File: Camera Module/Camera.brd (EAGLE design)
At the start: 39.7 x 23 mm, 7 parts, among them U2 RFM69HCW

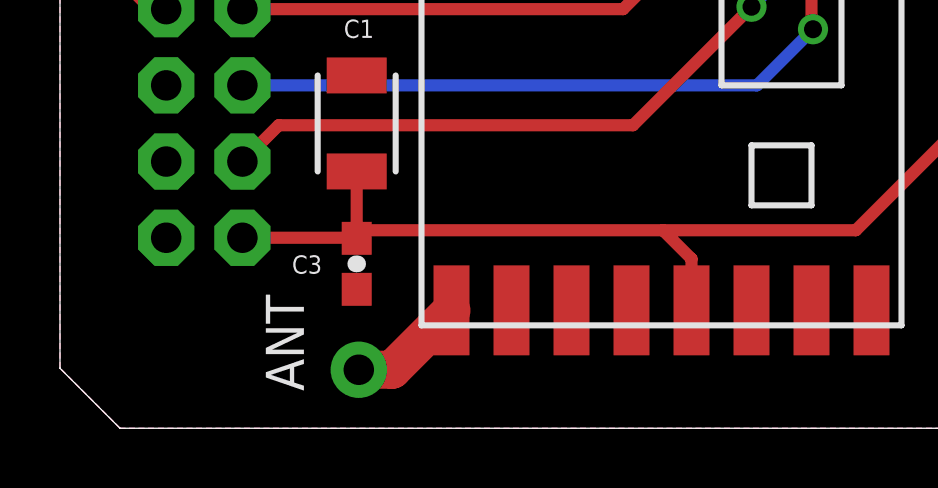
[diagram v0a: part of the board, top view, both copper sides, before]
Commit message: Added the interrupt line from the RFM69 into the Camera Module board. It is connected to GPIO_24
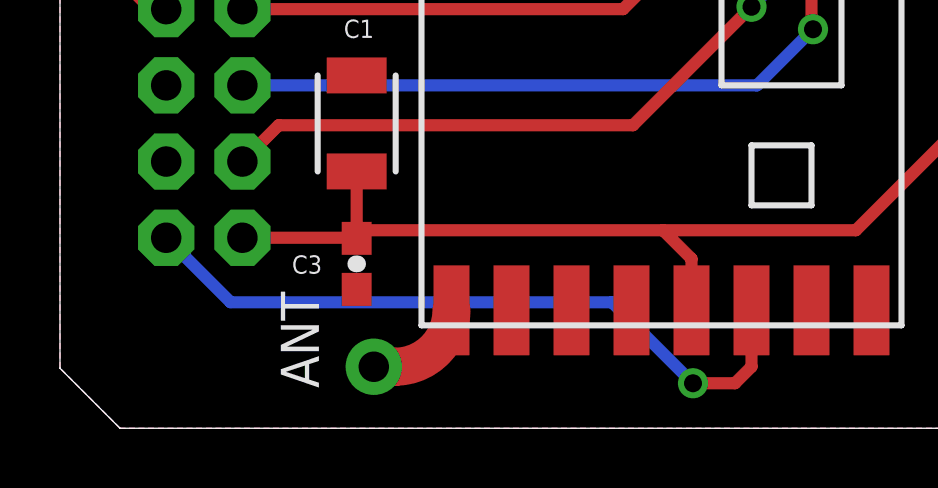
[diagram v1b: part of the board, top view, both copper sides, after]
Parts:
- moved ANT 0.51 mm to (10.5, 2.05)
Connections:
- new net INT: J1.2, U2.14
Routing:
- net INT: track 0.00 -> 23.6 mm, vias 0 -> 1
- net ANT: track 3.91 -> 3.37 mm
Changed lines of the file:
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@@
 </autorouter>
 <elements>
-<element name="ANT" library="SparkFun-Connectors" package="1X01_NO_SILK" value="" x="9.96" y="1.95" smashed="yes" rot="R90">
-<attribute name="NAME" x="8.1312" y="1.2438" size="1.27" layer="25" rot="R90"/>
-<attribute name="VALUE" x="13.135" y="0.68" size="1.27" layer="27" rot="R90"/>
+<element name="ANT" library="SparkFun-Connectors" package="1X01_NO_SILK" value="" x="10.46" y="2.05" smashed="yes" rot="R90">
+<attribute name="NAME" x="8.6312" y="1.3438" size="1.27" layer="25" rot="R90"/>
+<attribute name="VALUE" x="13.635" y="0.78" size="1.27" layer="27" rot="R90"/>
 </element>
 <element name="C1" library="SparkFun-Capacitors" package="1210" value="10uF" x="9.89" y="10.16" smashed="yes" rot="R90">
@@
 <contactref element="U2" pad="9"/>
 <contactref element="ANT" pad="1"/>
-<wire x1="9.96" y1="1.95" x2="11.07" y2="1.95" width="1.27" layer="1"/>
-<wire x1="11.07" y1="1.95" x2="13.05" y2="3.93" width="1.27" layer="1"/>
+<wire x1="10.46" y1="2.05" x2="11.17" y2="2.05" width="1.27" layer="1"/>
+<wire x1="11.17" y1="2.05" x2="13.05" y2="3.93" width="1.27" layer="1" curve="90"/>
 </signal>
 <signal name="MOSI">
@@
 <contactref element="J1" pad="10"/>
 </signal>
+<signal name="INT">
+<contactref element="U2" pad="14"/>
+<contactref element="J1" pad="2"/>
+<via x="21.1" y="1.5" extent="1-16" drill="0.6"/>
+<wire x1="23.05" y1="3.93" x2="23.05" y2="2.05" width="0.4064" layer="1"/>
+<wire x1="23.05" y1="2.05" x2="22.5" y2="1.5" width="0.4064" layer="1"/>
+<wire x1="22.5" y1="1.5" x2="21.1" y2="1.5" width="0.4064" layer="1"/>
+<wire x1="21.1" y1="1.5" x2="18.4" y2="4.2" width="0.4064" layer="16"/>
+<wire x1="18.4" y1="4.2" x2="5.69" y2="4.2" width="0.4064" layer="16"/>
+<wire x1="5.69" y1="4.2" x2="3.54" y2="6.35" width="0.4064" layer="16"/>
+</signal>
 </signals>

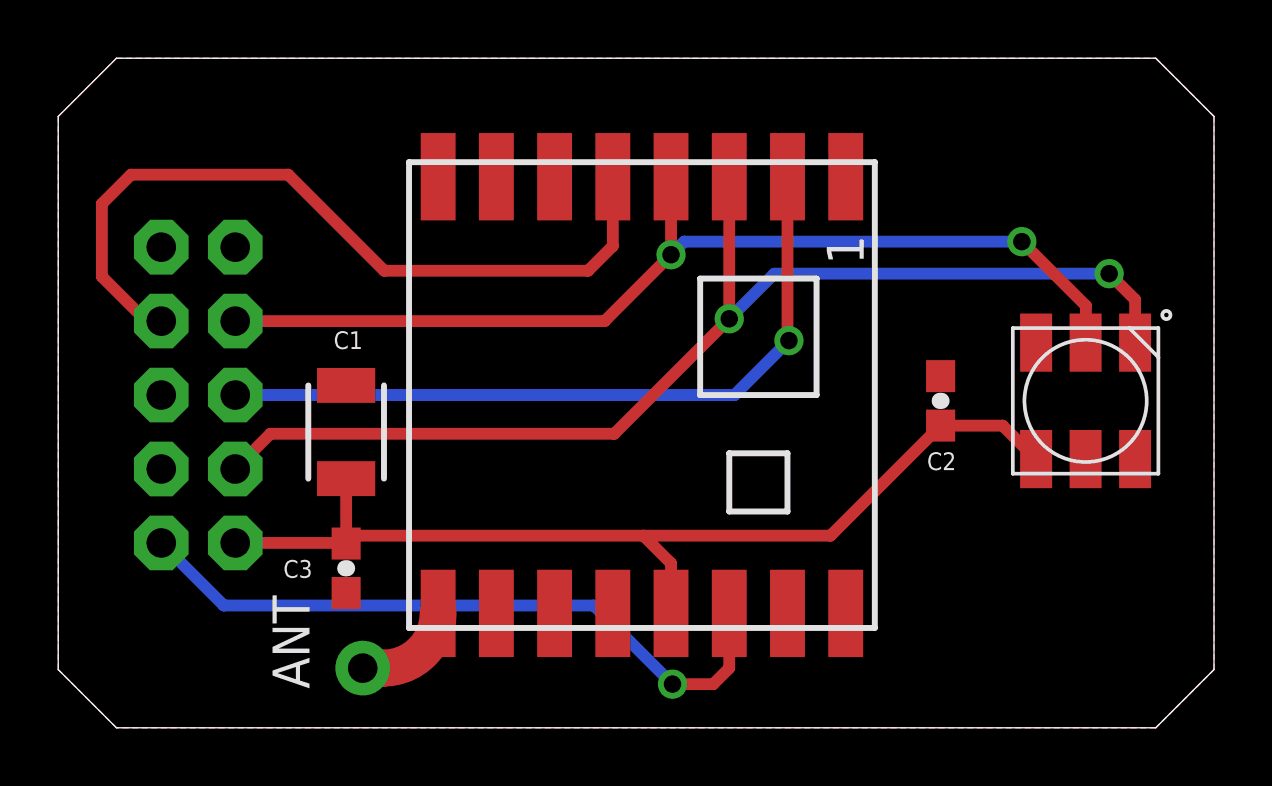
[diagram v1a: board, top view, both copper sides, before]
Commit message: Update the camera module board to include a chip select line for the APA102 and added to the silk screen
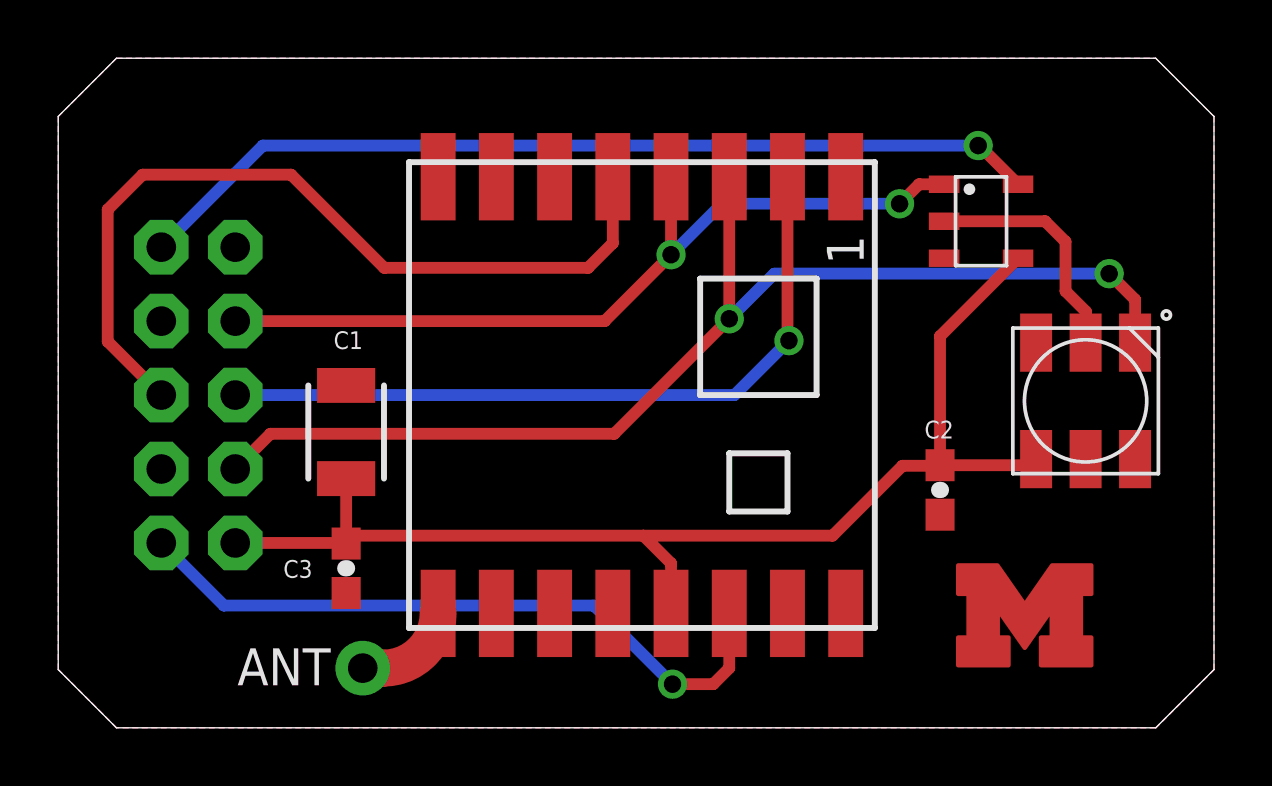
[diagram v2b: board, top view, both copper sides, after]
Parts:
- added U$2: TS12A4514, SAUVE:SOT-23
- added U$3: (no value), MAAV_BlockM:BLOCK-M-5MM-MASK
- added U$5: (no value), MAAV_BlockM:BLOCK-M-10MM
- moved C2 3.06 mm to (30.3, 8.17), turned to 270 degrees
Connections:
- net INT renamed GPIO24
- new net APA_SCLK: U$1.CKI, U$2.2
- new net GPIO25: J1.6, U2.5
- net 3.3V: now also U$2.4
- net CE0: no longer U2.5
- net CE1: now also U$2.5
- net GND: now also U$2.3
- net SCLK: now also U$2.1; no longer U$1.CKI
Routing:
- net CE1: track 0.00 -> 31.4 mm, vias 0 -> 1
- net GPIO25: track 0.00 -> 28.9 mm
- net CE0: track 27.2 -> 0.00 mm
- net APA_SCLK: track 0.00 -> 8.22 mm
- net 3.3V: track 35.0 -> 42.3 mm
- net SCLK: track 34.5 -> 29.0 mm
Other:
- board text added: "AIZER"
- board text added: "Camera Module"
- board text added: "Designed By: Matt Sauvé"

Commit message: Finalized all PCBs
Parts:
- added JP1: JUMPER-PAD-2-NC_BY_TRACE, SparkFun-Passives:PAD-JUMPER-2-NC_BY_TRACE_YES_SILK
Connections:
- net APA_SCLK: now also JP1.2
- net SCLK: now also JP1.1
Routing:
- net SCLK: track 29.0 -> 37.4 mm
- net APA_SCLK: track 8.22 -> 11.0 mm
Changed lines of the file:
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@@
 <wire x1="0" y1="2" x2="2" y2="0" width="0" layer="20"/>
 <text x="28.5" y="7.4" size="5.08" layer="22" ratio="12" rot="MR0">AIZER</text>
-<text x="38.6" y="5.5" size="1.27" layer="22" ratio="12" rot="MR0">Camera Module</text>
+<text x="38.6" y="5.1" size="1.27" layer="22" ratio="12" rot="MR0">Camera Module</text>
 <text x="37.1" y="1.3" size="0.6096" layer="22" ratio="10" rot="MR0">Designed By: Matt Sauvé</text>
 </plain>
@@
 </class>
 </classes>
-<designrules name="default">
+<designrules name="oshpark-2layer">
 <description language="de">&lt;b&gt;EAGLE Design Rules&lt;/b&gt;
 &lt;p&gt;
@@
 Einstellungen hier und speichern die Design Rules unter
 einem neuen Namen ab.</description>
-<description language="en">&lt;b&gt;EAGLE Design Rules&lt;/b&gt;
+<description language="en">&lt;b&gt;Laen's PCB Order Design Rules&lt;/b&gt;
 &lt;p&gt;
-The default Design Rules have been set to cover
-a wide range of applications. Your particular design
-may have different requirements, so please make the
-necessary adjustments and save your customized
-design rules under a new name.</description>
+Please make sure your boards conform to these design rules.</description>
 <param name="layerSetup" value="(1*16)"/>
-<param name="mtCopper" value="0.035mm 0.035mm 0.035mm 0.035mm 0.035mm 0.035mm 0.035mm 0.035mm 0.035mm 0.035mm 0.035mm 0.035mm 0.035mm 0.035mm 0.035mm 0.035mm"/>
-<param name="mtIsolate" value="1.5mm 0.15mm 0.2mm 0.15mm 0.2mm 0.15mm 0.2mm 0.15mm 0.2mm 0.15mm 0.2mm 0.15mm 0.2mm 0.15mm 0.2mm"/>
-<param name="mdWireWire" value="8mil"/>
-<param name="mdWirePad" value="8mil"/>
-<param name="mdWireVia" value="8mil"/>
-<param name="mdPadPad" value="8mil"/>
-<param name="mdPadVia" value="8mil"/>
-<param name="mdViaVia" value="8mil"/>
-<param name="mdSmdPad" value="8mil"/>
-<param name="mdSmdVia" value="8mil"/>
-<param name="mdSmdSmd" value="8mil"/>
+<param name="mtCopper" value="0.0356mm 0.0356mm 0.0356mm 0.0356mm 0.0356mm 0.0356mm 0.0356mm 0.0356mm 0.0356mm 0.0356mm 0.0356mm 0.0356mm 0.0356mm 0.0356mm 0.0356mm 0.0356mm"/>
+<param name="mtIsolate" value="1.5011mm 0.1499mm 0.2007mm 0.1499mm 0.2007mm 0.1499mm 0.2007mm 0.1499mm 0.2007mm 0.1499mm 0.2007mm 0.1499mm 0.2007mm 0.1499mm 0.2007mm"/>
+<param name="mdWireWire" value="6mil"/>
+<param name="mdWirePad" value="6mil"/>
+<param name="mdWireVia" value="6mil"/>
+<param name="mdPadPad" value="6mil"/>
+<param name="mdPadVia" value="6mil"/>
+<param name="mdViaVia" value="6mil"/>
+<param name="mdSmdPad" value="6mil"/>
+<param name="mdSmdVia" value="6mil"/>
+<param name="mdSmdSmd" value="6mil"/>
 <param name="mdViaViaSameLayer" value="8mil"/>
 <param name="mnLayersViaInSmd" value="2"/>
-<param name="mdCopperDimension" value="40mil"/>
-<param name="mdDrill" value="8mil"/>
+<param name="mdCopperDimension" value="15mil"/>
+<param name="mdDrill" value="6mil"/>
 <param name="mdSmdStop" value="0mil"/>
-<param name="msWidth" value="10mil"/>
-<param name="msDrill" value="24mil"/>
-<param name="msMicroVia" value="9.99mm"/>
+<param name="msWidth" value="6mil"/>
+<param name="msDrill" value="13mil"/>
+<param name="msMicroVia" value="13mil"/>
 <param name="msBlindViaRatio" value="0.5"/>
 <param name="rvPadTop" value="0.25"/>
@@
 <param name="rvMicroViaOuter" value="0.25"/>
 <param name="rvMicroViaInner" value="0.25"/>
-<param name="rlMinPadTop" value="10mil"/>
+<param name="rlMinPadTop" value="7mil"/>
 <param name="rlMaxPadTop" value="20mil"/>
-<param name="rlMinPadInner" value="10mil"/>
+<param name="rlMinPadInner" value="7mil"/>
 <param name="rlMaxPadInner" value="20mil"/>
-<param name="rlMinPadBottom" value="10mil"/>
+<param name="rlMinPadBottom" value="7mil"/>
 <param name="rlMaxPadBottom" value="20mil"/>
-<param name="rlMinViaOuter" value="8mil"/>
+<param name="rlMinViaOuter" value="7mil"/>
 <param name="rlMaxViaOuter" value="20mil"/>
-<param name="rlMinViaInner" value="8mil"/>
+<param name="rlMinViaInner" value="7mil"/>
 <param name="rlMaxViaInner" value="20mil"/>
 <param name="rlMinMicroViaOuter" value="4mil"/>
@@
 <param name="mvStopFrame" value="1"/>
 <param name="mvCreamFrame" value="0"/>
-<param name="mlMinStopFrame" value="4mil"/>
-<param name="mlMaxStopFrame" value="4mil"/>
+<param name="mlMinStopFrame" value="2.5mil"/>
+<param name="mlMaxStopFrame" value="2.5mil"/>
 <param name="mlMinCreamFrame" value="0mil"/>
 <param name="mlMaxCreamFrame" value="0mil"/>
@@
 <elements>
 <element name="ANT" library="SparkFun-Connectors" package="1X01_NO_SILK" value="" x="10.46" y="2.05" smashed="yes" rot="R90">
-<attribute name="NAME" x="9.3562" y="2.7312" size="1.27" layer="25" rot="R180"/>
+<attribute name="NAME" x="9.3562" y="2.7312" size="1.27" layer="25" ratio="12" rot="R180"/>
 <attribute name="VALUE" x="13.635" y="0.78" size="1.27" layer="27" rot="R90"/>
 </element>
 <element name="C1" library="SparkFun-Capacitors" package="1210" value="10uF" x="9.89" y="10.16" smashed="yes" rot="R90">
 <attribute name="PROD_ID" value="CAP-09824" x="9.89" y="10.16" size="1.778" layer="27" rot="R90" display="off"/>
-<attribute name="NAME" x="9.46" y="13.01" size="0.6096" layer="25"/>
+<attribute name="NAME" x="9.56" y="12.91" size="0.4064" layer="25" ratio="12"/>
 </element>
 <element name="C2" library="SparkFun-Capacitors" package="0603-CAP@1" value="0.1uF" x="30.29" y="8.17" smashed="yes" rot="R270">
 <attribute name="PROD_ID" value="CAP-00810" x="30.29" y="8.17" size="1.778" layer="27" rot="R270" display="off"/>
-<attribute name="NAME" x="30.759" y="10.548" size="0.6096" layer="25" font="vector" rot="R180"/>
+<attribute name="NAME" x="30.659" y="10.248" size="0.4064" layer="25" font="vector" ratio="12" rot="R180"/>
 </element>
 <element name="C3" library="SparkFun-Capacitors" package="0603-CAP@1" value="0.1uF" x="9.89" y="5.48" smashed="yes" rot="R270">
 <attribute name="PROD_ID" value="CAP-00810" x="9.89" y="5.48" size="1.778" layer="27" rot="R270" display="off"/>
-<attribute name="NAME" x="7.731" y="5.152" size="0.6096" layer="25" font="vector"/>
+<attribute name="NAME" x="8.131" y="5.252" size="0.4064" layer="25" font="vector" ratio="12"/>
 </element>
 <element name="J1" library="SparkFun-Connectors" package="2X5_NOSILK" value="" x="4.81" y="11.43" smashed="yes" rot="R180">
@@
 <element name="U$3" library="MAAV_BlockM" package="BLOCK-M-5MM-MASK" value="" x="33.2" y="3.8"/>
 <element name="U$5" library="MAAV_BlockM" package="BLOCK-M-10MM" value="" x="34.1" y="10.7" rot="MR0"/>
+<element name="JP1" library="SparkFun-Passives" package="PAD-JUMPER-2-NC_BY_TRACE_YES_SILK" value="JUMPER-PAD-2-NC_BY_TRACE" x="36.3" y="19.3" smashed="yes" rot="R270"/>
 </elements>
 <signals>
@@
 <wire x1="28.9" y1="18" x2="29.57" y2="18.67" width="0.4064" layer="1"/>
 <wire x1="29.57" y1="18.67" x2="30.43" y2="18.67" width="0.4064" layer="1"/>
+<contactref element="JP1" pad="1"/>
+<wire x1="36.3" y1="19.808" x2="34.908" y2="21.2" width="0.4064" layer="1"/>
+<wire x1="34.908" y1="21.2" x2="31.3" y2="21.2" width="0.4064" layer="1"/>
+<wire x1="31.3" y1="21.2" x2="30.43" y2="20.33" width="0.4064" layer="1"/>
+<wire x1="30.43" y1="20.33" x2="30.43" y2="18.67" width="0.4064" layer="1"/>
 </signal>
 <signal name="CE0">
@@
 <wire x1="35.3" y1="14.3" x2="35.3" y2="13.24" width="0.4064" layer="1"/>
 <wire x1="35.3" y1="13.24" x2="35.29" y2="13.23" width="0.4064" layer="1"/>
+<contactref element="JP1" pad="2"/>
+<wire x1="36.3" y1="18.792" x2="34.6" y2="17.092" width="0.4064" layer="1"/>
+<wire x1="34.6" y1="17.092" x2="34.6" y2="16.7" width="0.4064" layer="1"/>
 </signal>
 </signals>
